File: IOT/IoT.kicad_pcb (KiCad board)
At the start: 2 copper layers, 4.5 x 13.4 mm, 143 parts, among them IC1 MAX3222EAP+, IC2 MAX3222EAP+, J1 USB_C_Receptacle_USB2.0_16P, J10 Program header, J11 Conn_01x08_Pin, J12 Micro_SD_Card_Det2, J13 Conn_01x08_Pin, J14 Flow sensor, J15 RS232_1, J16 RS232_1, J17 24V, J18 12V, J19 5V, J2 Conn_01x01_Pin, J20 3V3, J3 Conn_01x04_Pin, J4 Conn_01x01_Pin, J5 Conn_01x02_Pin, J6 Conn_01x02_Pin, J7 Conn_01x01_Pin, J8 Conn_01x05_Pin, J9 Conn_01x03_Pin, SW1 SW_Push, SW2 SW_Push, SW3 SW_Push, SW4 SW_Push, SW5 SW_Push, U1 STM32F401RETx, U2 TPS5430DDA, U3 TPS5430DDA, U4 MCP73831-3-OT, U5 MT3608, U6 AMS1117-3.3, Y1 HSE, Y2 32.768khz

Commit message: started pcb
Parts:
- removed TP4: TestPoint_Flag, TestPoint:TestPoint_Pad_2.0x2.0mm
- added C32: 10u, Capacitor_SMD:C_0805_2012Metric_Pad1.18x1.45mm_HandSolder, F.Cu at (94.9, 150.1)
- added C33: 10u, Capacitor_SMD:C_0805_2012Metric_Pad1.18x1.45mm_HandSolder, F.Cu at (94.9, 153.1)
- added C34: 22u/10V, Capacitor_Tantalum_SMD:CP_EIA-3528-12_Kemet-T_HandSolder, F.Cu at (109.5, 163.1)
- added D10: LED, Capacitor_SMD:C_0805_2012Metric_Pad1.18x1.45mm_HandSolder, F.Cu at (94.9, 159.1)
- added D11: LED, Capacitor_SMD:C_0805_2012Metric_Pad1.18x1.45mm_HandSolder, F.Cu at (94.9, 162.1)
- added D15: LED, Diode_SMD:D_0805_2012Metric_Pad1.15x1.40mm_HandSolder, F.Cu at (102.1, 155.2)
- added D16: LED, Diode_SMD:D_0805_2012Metric_Pad1.15x1.40mm_HandSolder, F.Cu at (102.1, 158.2)
- added D9: LED, Capacitor_SMD:C_0805_2012Metric_Pad1.18x1.45mm_HandSolder, F.Cu at (94.9, 156.1)
- added R22: 10k, LED_SMD:LED_1206_3216Metric_Pad1.42x1.75mm_HandSolder, F.Cu at (75.1, 154.5)
- added R23: 2.2k, LED_SMD:LED_1206_3216Metric_Pad1.42x1.75mm_HandSolder, F.Cu at (75.1, 157.9)
- added R24: 1k, LED_SMD:LED_1206_3216Metric_Pad1.42x1.75mm_HandSolder, F.Cu at (75.1, 161.3)
- added R26: 10k, LED_SMD:LED_1206_3216Metric_Pad1.42x1.75mm_HandSolder, F.Cu at (81.1, 151.1)
- added R27: 1k, LED_SMD:LED_1206_3216Metric_Pad1.42x1.75mm_HandSolder, F.Cu at (81.1, 154.5)
- added R28: 470, LED_SMD:LED_1206_3216Metric_Pad1.42x1.75mm_HandSolder, F.Cu at (81.1, 157.9)
- added TP10: TestPoint, Connector_Pin:Pin_D0.7mm_L6.5mm_W1.8mm_FlatFork, F.Cu at (86.0, 158.0)
- added TP11: TestPoint, Connector_Pin:Pin_D0.7mm_L6.5mm_W1.8mm_FlatFork, F.Cu at (86.0, 161.5)
- added TP12: TestPoint, Connector_Pin:Pin_D0.7mm_L6.5mm_W1.8mm_FlatFork, F.Cu at (89.8, 151.1)
- added TP13: TestPoint, Connector_Pin:Pin_D0.7mm_L6.5mm_W1.8mm_FlatFork, F.Cu at (89.8, 154.6)
- added TP14: TestPoint, Connector_Pin:Pin_D0.7mm_L6.5mm_W1.8mm_FlatFork, F.Cu at (89.8, 158.0)
- added TP8: TestPoint, Connector_Pin:Pin_D0.7mm_L6.5mm_W1.8mm_FlatFork, F.Cu at (86.0, 151.1)
- added TP9: TestPoint, Connector_Pin:Pin_D0.7mm_L6.5mm_W1.8mm_FlatFork, F.Cu at (86.0, 154.6)
- added U4: MCP73831-3-OT, Package_TO_SOT_SMD:SOT-23-5, F.Cu at (108.8, 154.0)
- added U5: MT3608, Package_TO_SOT_SMD:SOT-23-6, F.Cu at (108.8, 158.7)
- BT1: moved to B.Cu
- C12, C13, C6: footprint Capacitor_SMD:CP_Elec_4x5.4 -> Capacitor_SMD:C_0805_2012Metric_Pad1.18x1.45mm_HandSolder
- C2, C3: value 18p -> 22p
- C29: value 47uF/16V -> 47uF/35V; footprint Capacitor_SMD:CP_Elec_6.3x5.4 -> Capacitor_SMD:CP_Elec_8x10
- C30: footprint Capacitor_SMD:CP_Elec_5x5.4 -> Capacitor_SMD:CP_Elec_8x10
- C34: value 22u -> 22u/10V; footprint Capacitor_Tantalum_SMD:CP_EIA-3216-12_Kemet-S_HandSolder -> Capacitor_Tantalum_SMD:CP_EIA-3528-12_Kemet-T_HandSolder
- D13, D7, D8: footprint Diode_SMD:D_SMB-SMC_Universal_Handsoldering -> Diode_SMD:D_SMA_Handsoldering
- D17, D18: footprint Diode_SMD:Littelfuse_PolyZen-LS -> Diode_SMD:D_1206_3216Metric_Pad1.42x1.75mm_HandSolder
- D19, D20: footprint Diode_SMD:Nexperia_DSN1608-2_1.6x0.8mm -> Diode_SMD:D_1206_3216Metric_Pad1.42x1.75mm_HandSolder
- IC1, IC2: footprint Library:SOP65P778X199-20N -> Package_SO:TSSOP-20_4.4x5mm_P0.4mm
- J10, J8: footprint Connector_PinSocket_2.54mm:PinSocket_1x05_P2.54mm_Horizontal -> Connector_PinSocket_2.54mm:PinSocket_1x05_P2.54mm_Vertical
- J11, J13: footprint Connector_PinSocket_2.54mm:PinSocket_1x08_P2.54mm_Horizontal -> Connector_PinSocket_2.54mm:PinSocket_1x08_P2.54mm_Vertical
- J14: footprint Package_SO:TSSOP-8_3x3mm_P0.65mm -> Connector_PinSocket_2.54mm:PinSocket_1x04_P2.54mm_Vertical
- J2, J4, J7: footprint Connector_PinSocket_2.54mm:PinSocket_1x01_P2.54mm_Horizontal -> Connector_PinSocket_2.54mm:PinSocket_1x01_P2.54mm_Vertical
- J3: footprint Connector_PinSocket_2.54mm:PinSocket_1x04_P2.54mm_Horizontal -> Connector_PinSocket_2.54mm:PinSocket_1x04_P2.54mm_Vertical
- J5, J6: footprint Connector_PinSocket_2.54mm:PinSocket_1x02_P2.54mm_Horizontal -> Connector_PinSocket_2.54mm:PinSocket_1x02_P2.54mm_Vertical
- J9: footprint Connector_PinSocket_2.54mm:PinSocket_1x03_P2.54mm_Horizontal -> Connector_PinSocket_2.54mm:PinSocket_1x03_P2.54mm_Vertical
- L1: value 22uH 2A -> 22uH 3A; footprint Inductor_SMD:L_Wuerth_WE-PD2-Typ-L -> Inductor_SMD:L_Wuerth_WE-PD-Typ-LS_Handsoldering
- L2: footprint Inductor_SMD:L_Wuerth_WE-PD2-Typ-L -> Inductor_SMD:L_Wuerth_WE-PD-Typ-LS_Handsoldering
- L3: footprint Inductor_SMD:L_Wuerth_WE-PD-Typ-M-Typ-S_Handsoldering -> Inductor_SMD:L_Changjiang_FXL0615
- R1, R10, R11, R12, R13, R14, R15, R17, R19, R2, R20, R22, R23, R24, R25, R26, R27, R28, R3, R4, R5, R6, R7, R8, R9: footprint Resistor_SMD:R_0805_2012Metric_Pad1.20x1.40mm_HandSolder -> LED_SMD:LED_1206_3216Metric_Pad1.42x1.75mm_HandSolder
- R16: value 4.8k -> 4.7k; footprint Resistor_SMD:R_0805_2012Metric_Pad1.20x1.40mm_HandSolder -> LED_SMD:LED_1206_3216Metric_Pad1.42x1.75mm_HandSolder
- R18: value 3.8k -> nbt; footprint Resistor_SMD:R_0805_2012Metric_Pad1.20x1.40mm_HandSolder -> LED_SMD:LED_1206_3216Metric_Pad1.42x1.75mm_HandSolder
- R21: value 88.7k -> 120k//330k; footprint Resistor_SMD:R_0805_2012Metric_Pad1.20x1.40mm_HandSolder -> LED_SMD:LED_1206_3216Metric_Pad1.42x1.75mm_HandSolder
- SW1, SW2, SW3, SW4, SW5: footprint Button_Switch_SMD:Panasonic_EVQPUJ_EVQPUA -> Button_Switch_SMD:SW_DIP_SPSTx01_Slide_6.7x4.1mm_W6.73mm_P2.54mm_LowProfile_JPin
- TP1, TP2, TP3, TP5, TP6, TP7: footprint TestPoint:TestPoint_Pad_2.0x2.0mm -> Connector_Pin:Pin_D0.7mm_L6.5mm_W1.8mm_FlatFork
- Y1: value HSE -> 16MHz; footprint Crystal:Crystal_SMD_5032-2Pin_5.0x3.2mm_HandSoldering -> Crystal:Crystal_SMD_Abracon_ABM8AIG-4Pin_3.2x2.5mm
- moved U4 332.6 mm to (78.2, 123.8), turned to 90 degrees
- moved D9 330.2 mm to (77.3, 129.4), turned to 180 degrees
- moved L3 324.1 mm to (94.5, 129.2)
- moved C28 323.4 mm to (71.9, 124.7), turned to -90 degrees
- moved C30 318.3 mm to (80.5, 107.6)
- moved C31 318.2 mm to (83.2, 125.1), turned to -90 degrees
- moved U5 315.5 mm to (94.6, 123.3), turned to 180 degrees
- moved D13 314.6 mm to (102.1, 121.9), turned to -90 degrees
- moved C27 314.4 mm to (77.5, 95.6), turned to 90 degrees
- moved R17 309.7 mm to (72.9, 129.4), turned to 180 degrees
- moved L2 309.6 mm to (69.8, 97.3), turned to -90 degrees
- moved D15 306.5 mm to (106.5, 127.1), turned to 90 degrees
- moved D12 304.0 mm to (98.8, 106.2), turned to -90 degrees
- moved D11 303.9 mm to (97.6, 95.5), turned to -90 degrees
- moved R18 303.3 mm to (75.3, 120.4), turned to 90 degrees
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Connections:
- net Net-(BT1-+) renamed /Power/Vbat
- C26 pad 1: Net-(D7-K) -> Net-(U2-BOOT)
- C26 pad 2: Net-(U2-PH) -> Net-(D7-K)
- C27 pad 1: Net-(D8-K) -> Net-(U3-BOOT)
- C27 pad 2: Net-(U3-PH) -> Net-(D8-K)
- U2 pad 1: Net-(D7-K) -> Net-(U2-BOOT)
- U2 pad 8: Net-(U2-PH) -> Net-(D7-K)
- U3 pad 1: Net-(D8-K) -> Net-(U3-BOOT)
- U3 pad 8: Net-(U3-PH) -> Net-(D8-K)
- Y1 pad 1: Net-(U1-PH1) -> Net-(U1-PH0)
- Y1 pad 2: Net-(U1-PH0) -> GND
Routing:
- net /Power/5V_Buck: track 0.00 -> 75.5 mm
- net Net-(D13-K): track 0.00 -> 30.1 mm
- net GND: track 0.00 -> 29.8 mm, vias 0 -> 8
- net +3V3: track 0.00 -> 23.6 mm
- net Net-(U1-PH0): track 0.00 -> 17.0 mm
- net Net-(J17-Pin_1): track 0.00 -> 12.5 mm
- net Net-(U1-PH1): track 0.00 -> 10.4 mm
- net Net-(U1-PC15): track 0.00 -> 10.1 mm
- net /Power/Vbat: track 0.00 -> 10.1 mm
- net Net-(U1-PC14): track 0.00 -> 9.41 mm
- net +5V: track 0.00 -> 7.59 mm
- net Net-(U1-VCAP1): track 0.00 -> 6.35 mm
- net Net-(D7-K): track 0.00 -> 5.27 mm
- net /5V available: track 0.00 -> 5.12 mm
- net Net-(U2-VSENSE): track 0.00 -> 5.10 mm
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- added copper zone on F.Cu, net +12V
- added copper zone on F.Cu, net /Power/5V_Buck
- added copper zone on F.Cu, net /Power/Vbat
- added copper zone on B.Cu, net GND
- added copper zone on F.Cu, net GND
- added copper zone on F.Cu, net Net-(D13-A)
- added copper zone on F.Cu, net Net-(D7-K)
- added copper zone on F.Cu, net Net-(D8-K)
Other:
- board size 4.5 x 13.4 mm -> 272.3 x 127.9 mm

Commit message: update pcb with outline and tighter placemetn
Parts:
- removed the C32 at (106.5, 118.0)
- removed the C33 at (119.3, 120.0)
- removed the C34 at (124.3, 119.5)
- removed the D10 at (99.3, 76.2)
- removed the D11 at (97.6, 95.5)
- removed the D15 at (106.5, 127.1)
- removed the D16 at (120.0, 116.3)
- removed the D9 at (77.3, 129.4)
- removed the R22 at (84.8, 76.8)
- removed the R23 at (99.3, 71.3)
- removed the R24 at (97.6, 99.9)
- removed the R26 at (93.5, 120.4)
- removed the R27 at (106.7, 122.7)
- removed the R28 at (124.5, 116.3)
- removed the TP10 at (83.3, 117.7)
- removed the TP11 at (99.3, 66.5)
- removed the TP12 at (103.5, 100.1)
- removed the TP13 at (90.4, 116.6)
- removed the TP14 at (126.0, 113.7)
- removed the TP8 at (92.7, 67.7)
- removed the TP9 at (92.8, 108.6)
- removed the U4 at (78.2, 123.8)
- removed the U5 at (94.6, 123.3)
- moved TP11 96.9 mm to (93.5, 64.9), turned to 180 degrees
- moved R23 89.7 mm to (99.2, 71.5), turned to -90 degrees
- moved BT1 84.8 mm to (106.7, 64.3), turned to -90 degrees
- moved D10 83.0 mm to (99.3, 76.2), turned to 90 degrees
- moved TP8 82.9 mm to (92.3, 68.5), turned to 180 degrees
- moved R22 78.3 mm to (85.2, 76.8)
- moved D11 66.9 mm to (97.5, 95.2), turned to -90 degrees
- moved R24 65.3 mm to (97.7, 99.9), turned to 90 degrees
- moved R28 60.0 mm to (124.3, 116.3), turned to 180 degrees
- moved TP14 56.9 mm to (125.7, 113.9), turned to 180 degrees
- moved TP12 56.1 mm to (92.8, 95.1), turned to 180 degrees
- moved J10 52.2 mm to (205.4, 67.9)
- moved TP9 46.8 mm to (92.8, 108.3), turned to 180 degrees
- moved C34 46.3 mm to (124.3, 119.3)
- moved D16 45.6 mm to (119.9, 116.2)
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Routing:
- net Net-(D13-K): track 30.1 -> 23.3 mm
- net GND: track 29.8 -> 35.3 mm
- net Net-(D9-A): track 1.92 -> 0.00 mm
- net /Power/5V_Buck: track 75.5 -> 77.4 mm
- net Net-(D15-A): track 1.99 -> 0.18 mm
- net /Power/Vbat: track 10.1 -> 8.31 mm
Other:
- board size 272.3 x 127.9 mm -> 145.9 x 93.7 mm

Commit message: routed full pcb
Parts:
- removed J5, J6: Conn_01x02_Pin, Connector_PinSocket_2.54mm:PinSocket_1x02_P2.54mm_Vertical
- removed J7: Conn_01x01_Pin, Connector_PinSocket_2.54mm:PinSocket_1x01_P2.54mm_Vertical
- removed J8: Conn_01x05_Pin, Connector_PinSocket_2.54mm:PinSocket_1x05_P2.54mm_Vertical
- removed J9: Conn_01x03_Pin, Connector_PinSocket_2.54mm:PinSocket_1x03_P2.54mm_Vertical
- added H1: MountingHole, MountingHole:MountingHole_5.3mm_M5_ISO14580, F.Cu at (197.3, 51.4)
- added H2: MountingHole, MountingHole:MountingHole_5.3mm_M5_ISO14580, F.Cu at (197.3, 135.8)
- added H3: MountingHole, MountingHole:MountingHole_5.3mm_M5_ISO14580, F.Cu at (66.4, 135.8)
- added H4: MountingHole, MountingHole:MountingHole_5.3mm_M5_ISO14580, F.Cu at (66.6, 51.5)
- added J21: heated blanket, TerminalBlock_Philmore:TerminalBlock_Philmore_TB132_1x02_P5.00mm_Horizontal, F.Cu at (90.0, 135.3)
- added Q1: AO3400A, Package_TO_SOT_SMD:SOT-23, F.Cu at (95.6, 133.7)
- J1: footprint Connector_USB:USB_C_Receptacle_Amphenol_12401948E412A -> Connector_USB:USB_C_Receptacle_G-Switch_GT-USB-7010ASV
- J2: value Conn_01x01_Pin -> Conn_01x20_Pin; footprint Connector_PinSocket_2.54mm:PinSocket_1x01_P2.54mm_Vertical -> Connector_PinHeader_2.54mm:PinHeader_1x20_P2.54mm_Vertical
- J4: value Conn_01x01_Pin -> Conn_01x04_Pin; footprint Connector_PinSocket_2.54mm:PinSocket_1x01_P2.54mm_Vertical -> Connector_PinSocket_2.54mm:PinSocket_1x04_P2.54mm_Vertical
- moved J18 82.9 mm to (79.0, 135.3), turned to 180 degrees
- moved BT1 72.6 mm to (106.4, 136.9), turned to 90 degrees
- moved J13 72.1 mm to (199.7, 123.6), turned to -90 degrees
- moved JP4 68.2 mm to (176.8, 118.3), turned to 0 degrees
- moved JP3 62.4 mm to (176.6, 115.2), turned to 0 degrees
- moved J11 60.2 mm to (199.7, 110.3), turned to -90 degrees
- moved R13 50.2 mm to (147.3, 125.5)
- moved C13 43.9 mm to (182.9, 113.1), turned to 180 degrees
- moved J10 43.5 mm to (164.9, 83.6), turned to -90 degrees
- moved J2 36.1 mm to (199.5, 57.9), turned to 0 degrees
- moved U6 34.2 mm to (108.0, 94.9), turned to 180 degrees
- moved C33 29.5 mm to (113.4, 91.2), turned to 90 degrees
- moved C34 25.1 mm to (114.3, 96.3), turned to -90 degrees
- moved D16 24.5 mm to (117.3, 91.8), turned to -90 degrees
- moved R2 22.4 mm to (125.8, 126.3)
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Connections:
- net Net-(J17-Pin_1) renamed /Power/VIN
- J2 pad 1: Net-(J2-Pin_1) -> /PA0
- J3 pad 1: Net-(J3-Pin_1) -> +3V3
- J3 pad 2: Net-(J3-Pin_2) -> +3V3
- J3 pad 3: Net-(J3-Pin_3) -> +3V3
- J3 pad 4: Net-(J3-Pin_4) -> +3V3
- J4 pad 1: Net-(J4-Pin_1) -> GND
- R1 pad 1: /PB1 -> /BUTT1
- R2 pad 1: /PB2 -> /BUTT2
- R3 pad 1: /PB3 -> /BUTT3
- SW1 pad 1: /PB1 -> /BUTT1
- SW2 pad 1: /PB2 -> /BUTT2
- SW3 pad 1: /PB3 -> /BUTT3
- U1 pad 10: Net-(J3-Pin_3) -> /PC2
- U1 pad 11: Net-(J3-Pin_4) -> /PC3
- U1 pad 14: Net-(J5-Pin_1) -> /PA0
- U1 pad 15: Net-(J5-Pin_2) -> /PA1
- U1 pad 2: Net-(J4-Pin_1) -> /PC13
- U1 pad 20: unconnected-(U1-PA4-Pad20) -> /PA4
- U1 pad 25: unconnected-(U1-PC5-Pad25) -> /PC5
- U1 pad 26: Net-(J8-Pin_1) -> /PB0
- U1 pad 27: Net-(J8-Pin_2) -> /PB1
- U1 pad 28: Net-(J8-Pin_3) -> /PB2
- U1 pad 29: Net-(J9-Pin_3) -> /PB10
- U1 pad 42: Net-(J6-Pin_1) -> /PA9
- U1 pad 43: Net-(J6-Pin_2) -> /PA10
- U1 pad 50: Net-(J7-Pin_1) -> /PA15
- U1 pad 51: /PB1 -> /BUTT1
- U1 pad 52: /PB2 -> /BUTT2
- U1 pad 53: /PB3 -> /BUTT3
- U1 pad 54: Net-(J2-Pin_1) -> /PWMBlanket
- U1 pad 55: Net-(J8-Pin_4) -> /PB3
- U1 pad 56: Net-(J8-Pin_5) -> /PB4
- U1 pad 61: Net-(J9-Pin_1) -> /BP8
- U1 pad 62: Net-(J9-Pin_2) -> /PB9
- U1 pad 8: Net-(J3-Pin_1) -> /PC0
- U1 pad 9: Net-(J3-Pin_2) -> /PC1
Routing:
- net +3V3: track 23.6 -> 384.6 mm, vias 0 -> 9
- net +5V: track 7.59 -> 159.3 mm, vias 0 -> 3
- net /PA0: track 0.00 -> 119.3 mm, vias 0 -> 4
- net /PA1: track 0.00 -> 113.6 mm, vias 0 -> 4
- net /PWMBlanket: track 0.00 -> 98.3 mm, vias 0 -> 2
- net +12V: track 0.00 -> 97.0 mm, vias 0 -> 3
- net /NRST: track 0.00 -> 84.3 mm, vias 0 -> 1
- net /BUTT1: track 0.00 -> 79.1 mm, vias 0 -> 2
- net /PC3: track 0.00 -> 78.4 mm, vias 0 -> 2
- net /PC2: track 0.00 -> 75.6 mm, vias 0 -> 2
- net /BUTT2: track 0.00 -> 72.5 mm, vias 0 -> 2
- net /PC1: track 0.00 -> 72.3 mm, vias 0 -> 2
- net /PA4: track 0.00 -> 70.6 mm, vias 0 -> 2
- net /PC0: track 0.00 -> 70.5 mm, vias 0 -> 2
- net /PB0: track 0.00 -> 70.1 mm, vias 0 -> 3
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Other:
- board size 145.9 x 93.7 mm -> 140.1 x 93.7 mm

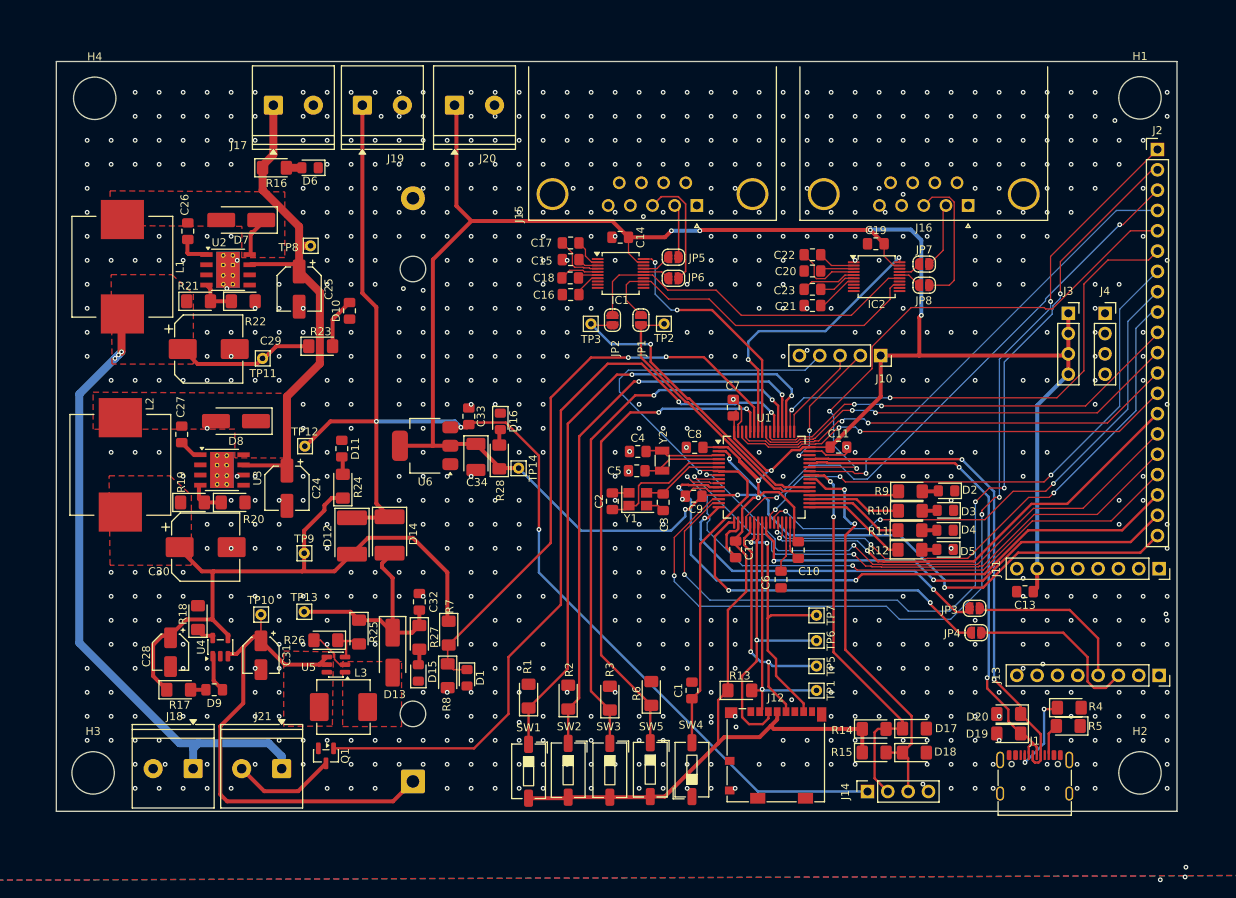
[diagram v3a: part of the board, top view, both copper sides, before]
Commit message: added silkscreen and updated footprints
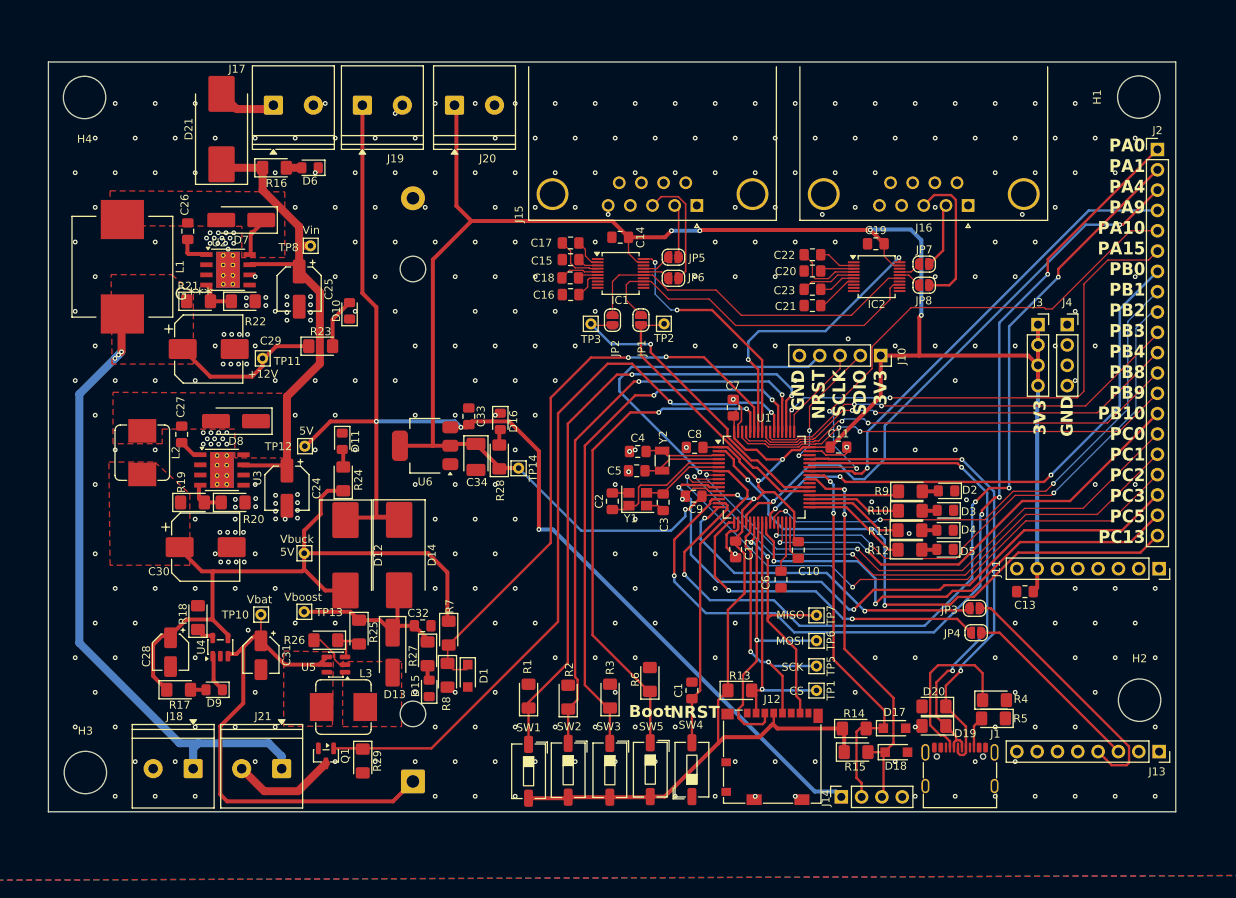
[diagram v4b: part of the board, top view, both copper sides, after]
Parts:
- added D21: low Vf, Diode_SMD:D_SMC_Handsoldering, F.Cu at (82.5, 55.3)
- added G***: LOGO, LOGO, B.Cu at (79.0, 75.9)
- added R29: 10k, LED_SMD:LED_1206_3216Metric_Pad1.42x1.75mm_HandSolder, F.Cu at (100.2, 134.3)
- D1: footprint Diode_SMD:D_0805_2012Metric_Pad1.15x1.40mm_HandSolder -> Diode_SMD:Nexperia_CFP3_SOD-123W
- D10, D11, D9: footprint Capacitor_SMD:C_0805_2012Metric_Pad1.18x1.45mm_HandSolder -> Diode_SMD:D_0805_2012Metric_Pad1.15x1.40mm_HandSolder
- D12, D14: footprint Diode_SMD:D_2114_3652Metric_Pad1.85x3.75mm_HandSolder -> Diode_SMD:D_SMC_Handsoldering
- D17, D18: footprint Diode_SMD:D_1206_3216Metric_Pad1.42x1.75mm_HandSolder -> Diode_SMD:Nexperia_CFP3_SOD-123W
- L2: footprint Inductor_SMD:L_Wuerth_WE-PD-Typ-LS_Handsoldering -> Inductor_SMD:L_Bourns_SRP7028A_7.3x6.6mm
- L3: footprint Inductor_SMD:L_Changjiang_FXL0615 -> Inductor_SMD:L_Bourns_SRP7028A_7.3x6.6mm
- moved J13 9.52 mm to (199.7, 133.1)
- moved J1 9.39 mm to (174.8, 136.3)
- moved R5 9.39 mm to (179.0, 129.0)
- moved D19 9.39 mm to (171.6, 129.9)
- moved D20 9.39 mm to (171.6, 127.5)
- moved R4 9.39 mm to (179.1, 126.7)
- moved H2 9.09 mm to (197.3, 126.7)
- moved J4 4.93 mm to (188.2, 79.8)
- moved J3 4.05 mm to (184.6, 79.8)
- moved J14 3.34 mm to (160.0, 138.8)
- moved L2 3.14 mm to (72.6, 95.8)
- moved C32 3.03 mm to (107.6, 117.4), turned to 0 degrees
- moved D14 2.78 mm to (104.7, 108.6)
- moved D12 2.55 mm to (98.0, 108.6)
- moved D17 2.49 mm to (166.6, 130.2)
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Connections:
- J17 pad 1: /Power/VIN -> Net-(D21-A)
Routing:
- net +3V3: track 384.6 -> 371.3 mm
- net /NB_RX: track 21.0 -> 32.5 mm
- net Net-(J1-CC1): track 10.6 -> 21.6 mm, vias 2 -> 0
- net Net-(D21-A): track 0.00 -> 7.47 mm
- net /PC13: track 66.6 -> 72.8 mm
- net Net-(D13-K): track 28.5 -> 23.5 mm
- net +5V: track 159.3 -> 154.6 mm
- net /Power/5V_Buck: track 80.6 -> 85.3 mm
- net /PC5: track 57.7 -> 61.8 mm
- net /PWMBlanket: track 98.3 -> 95.1 mm
- net /PC3: track 78.4 -> 81.4 mm
- net /Power/VIN: track 65.0 -> 62.5 mm
- net /PA4: track 70.6 -> 73.0 mm
- net +12V: track 97.0 -> 98.8 mm
- net /PA9: track 58.2 -> 59.9 mm
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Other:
- board size 140.1 x 93.7 mm -> 140.9 x 93.7 mm
- board text added: "+12V"
- board text added: "+5V GND"
- board text added: "+5V SCL SDA GND"
- board text added: "12V GND"
- board text added: "3V3"
- board text added: "3V3 GND"
- board text added: "5V"
- board text added: "Boot"
- board text added: "CS"
- board text added: "GND"
- board text added: "GND NRST SCLK SDIO 3V3"
- board text added: "IoT project Scheetmeters 2026, 2027 Lars Deprez, Lee Lauwereys, Maxime de Ryckel, Bram Van Oudenhove, Toon Van Havermaet, Simon Vandererven"
- board text added: "MISO"
- board text added: "MOSI"
- board text added: "NRST"
- board text added: "PA0 PA1 PA4 PA9 PA10 PA15 PB0 PB1 PB2 PB3 PB4 PB8 PB9 PB10 PC0 PC1 PC2 PC3 PC5 PC13"
- board text added: "PWM GND"
- board text added: "SCK"
- board text added: "V0.1"
- board text added: "VIN GND"
- board text added: "Vbat"
- board text added: "Vboost"
- board text added: "Vbuck 5V"
- board text added: "Vin"

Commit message: update PCB and schematic with components we can order
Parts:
- added D22: SK34, Diode_SMD:D_SMA_Handsoldering, B.Cu at (94.1, 135.0)
- U5: value MT3608 -> TPS61040DBVR
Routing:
- net Net-(D22-A): track 13.1 -> 24.0 mm
- net +12V: track 98.8 -> 104.1 mm
